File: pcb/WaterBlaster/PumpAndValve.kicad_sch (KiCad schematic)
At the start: 12 parts, among them J21 Conn_01x03, Q2 353-MCU60N02-TPCT-ND

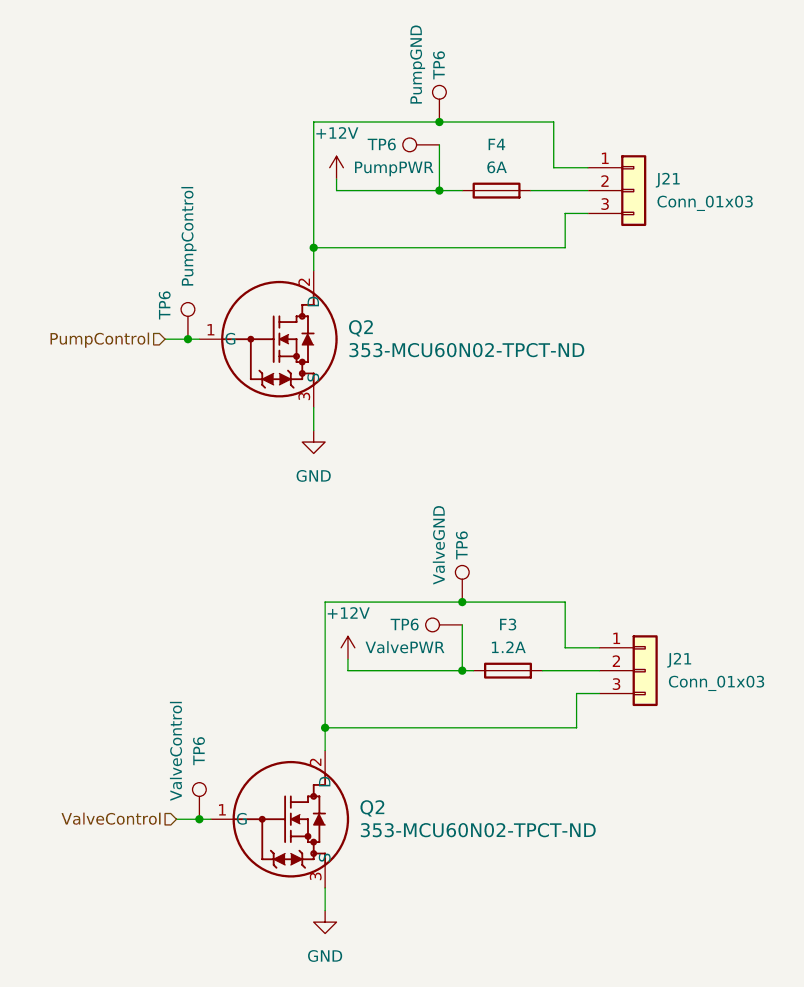
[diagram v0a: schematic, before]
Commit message: Updating firmware and CAD
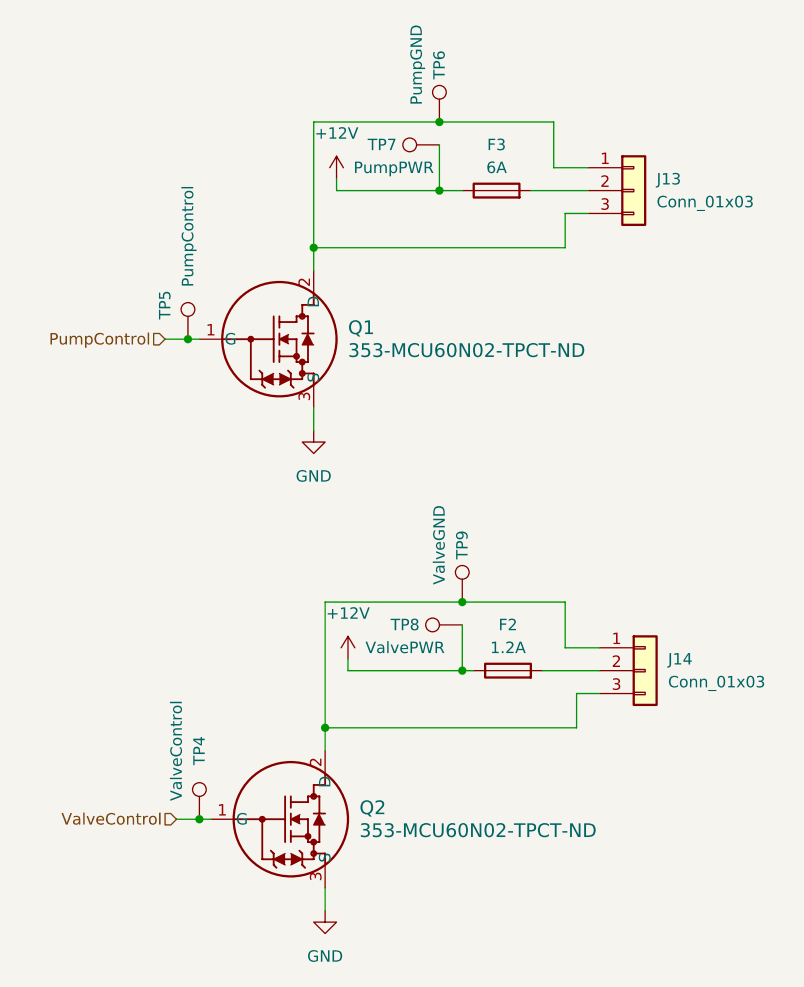
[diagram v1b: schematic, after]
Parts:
- renumbered F3 to F2, F4 to F3, J21 to J13, J21 to J14, Q2 to Q1, TP6 to TP4, TP6 to TP5, TP6 to TP7, TP6 to TP8, TP6 to TP9
